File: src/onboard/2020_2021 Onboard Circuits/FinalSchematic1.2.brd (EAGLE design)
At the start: 135.6 x 80 mm, 99 parts, among them IC1 A5975D, IC2 A5975D, IC3 A5975D

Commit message: Removed 5V lines as one layer is a 5V pour so they were not needed because the components are through hole. Then updated photos of both boards
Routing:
- net 5V: track 329.9 -> 3.95 mm, vias 2 -> 0
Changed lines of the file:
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@@
 <vertex x="-35.56" y="78.105" curve="-90"/>
 </polygon>
-<via x="40.64" y="43.18" extent="1-16" drill="0.35"/>
 <contactref element="R52" pad="2"/>
 <contactref element="C12" pad="1"/>
 <contactref element="5V" pad="1"/>
 <contactref element="L2" pad="1"/>
-<wire x1="88.9" y1="73.66" x2="98.8824" y2="63.6776" width="0.2032" layer="1"/>
-<wire x1="98.8824" y1="36.6524" x2="97.79" y2="35.56" width="0.2032" layer="1"/>
-<wire x1="97.79" y1="35.56" x2="97.79" y2="34.29" width="0.2032" layer="1"/>
-<wire x1="98.8824" y1="63.6776" x2="98.8824" y2="36.6524" width="0.2032" layer="1"/>
-<wire x1="45.72" y1="55.63" x2="48.1076" y2="53.2424" width="0.2032" layer="16"/>
-<wire x1="48.1076" y1="53.2424" x2="48.1076" y2="48.4124" width="0.2032" layer="16"/>
-<wire x1="48.1076" y1="48.4124" x2="42.8752" y2="43.18" width="0.2032" layer="16"/>
-<wire x1="42.8752" y1="43.18" x2="40.64" y2="43.18" width="0.2032" layer="16"/>
 <contactref element="DIP_1_2" pad="3"/>
-<wire x1="34.827" y1="36.656" x2="34.827" y2="32.483" width="0.2032" layer="1"/>
-<wire x1="34.827" y1="36.656" x2="34.827" y2="36.83" width="0.2032" layer="1"/>
-<wire x1="34.827" y1="36.83" x2="34.827" y2="37.367" width="0.2032" layer="1"/>
-<wire x1="34.827" y1="37.367" x2="40.64" y2="43.18" width="0.2032" layer="1"/>
-<wire x1="88.9" y1="26.67" x2="88.9" y2="24.13" width="0.3048" layer="16"/>
-<wire x1="86.3882" y1="21.6182" x2="86.3882" y2="9.1158" width="0.3048" layer="16"/>
-<wire x1="90.17" y1="5.334" x2="86.3882" y2="9.1158" width="0.3048" layer="16"/>
-<wire x1="90.17" y1="5.334" x2="90.17" y2="3.81" width="0.3048" layer="16"/>
-<wire x1="88.9" y1="24.13" x2="86.3882" y2="21.6182" width="0.3048" layer="16"/>
-<wire x1="54.61" y1="19.05" x2="50.8" y2="22.86" width="0.3048" layer="1"/>
-<wire x1="50.8" y1="22.86" x2="50.8" y2="24.13" width="0.3048" layer="1"/>
-<wire x1="50.8" y1="24.13" x2="48.67829375" y2="24.13" width="0.3048" layer="1"/>
-<wire x1="48.67829375" y1="24.13" x2="47.48449375" y2="25.3238" width="0.3048" layer="1"/>
-<wire x1="47.48449375" y1="25.3238" x2="41.9862" y2="25.3238" width="0.3048" layer="1"/>
-<wire x1="41.9862" y1="25.3238" x2="34.827" y2="32.483" width="0.3048" layer="1"/>
-<wire x1="34.827" y1="32.483" x2="34.827" y2="36.83" width="0.3048" layer="1"/>
-<wire x1="26.6708" y1="28.6738" x2="34.827" y2="36.83" width="0.3048" layer="1"/>
-<wire x1="17.2438" y1="28.6738" x2="26.6708" y2="28.6738" width="0.3048" layer="1"/>
-<wire x1="10.16" y1="16.51" x2="10.16" y2="21.59" width="0.3048" layer="1"/>
-<wire x1="10.16" y1="21.59" x2="-6.35" y2="38.1" width="0.3048" layer="1"/>
-<wire x1="-6.35" y1="38.1" x2="-10.16" y2="38.1" width="0.3048" layer="1"/>
-<wire x1="-10.16" y1="38.1" x2="-12.7" y2="38.1" width="0.3048" layer="1"/>
-<wire x1="-16.01550625" y1="36.9062" x2="-17.00449375" y2="36.9062" width="0.3048" layer="1"/>
-<wire x1="-12.7" y1="38.1" x2="-14.82170625" y2="38.1" width="0.3048" layer="1"/>
-<wire x1="-18.19829375" y1="38.1" x2="-20.32" y2="38.1" width="0.3048" layer="1"/>
-<wire x1="-14.82170625" y1="38.1" x2="-16.01550625" y2="36.9062" width="0.3048" layer="1"/>
-<wire x1="-17.00449375" y1="36.9062" x2="-18.19829375" y2="38.1" width="0.3048" layer="1"/>
 <wire x1="-20.32" y1="38.1" x2="-22.843" y2="38.1" width="0.3048" layer="1"/>
 <wire x1="-22.843" y1="38.1" x2="-23.715" y2="38.972" width="0.3048" layer="1"/>
-<via x="20.32" y="15.24" extent="1-16" drill="0.35"/>
-<wire x1="20.32" y1="15.24" x2="20.4343" y2="15.3543" width="0.3048" layer="16"/>
-<wire x1="20.4343" y1="15.3543" x2="33.4987125" y2="15.3543" width="0.3048" layer="16"/>
-<wire x1="53.34" y1="17.78" x2="35.9244125" y2="17.78" width="0.3048" layer="16"/>
-<wire x1="33.4987125" y1="15.3543" x2="35.9244125" y2="17.78" width="0.3048" layer="16"/>
-<wire x1="54.61" y1="19.05" x2="53.34" y2="17.78" width="0.3048" layer="16"/>
-<wire x1="16.74225" y1="15.24" x2="8.89" y2="7.38775" width="0.3048" layer="1"/>
-<wire x1="8.89" y1="7.38775" x2="8.89" y2="3.556" width="0.3048" layer="1"/>
-<wire x1="16.74225" y1="15.24" x2="20.32" y2="15.24" width="0.3048" layer="1"/>
-<wire x1="97.79" y1="34.29" x2="92.0496" y2="28.5496" width="0.3048" layer="16"/>
-<wire x1="92.0496" y1="28.5496" x2="90.97706875" y2="28.5496" width="0.3048" layer="16"/>
 <wire x1="89.09746875" y1="26.67" x2="88.9" y2="26.67" width="0.3048" layer="16"/>
-<wire x1="90.97706875" y1="28.5496" x2="89.09746875" y2="26.67" width="0.3048" layer="16"/>
-<wire x1="88.9" y1="26.67" x2="83.2838" y2="21.0538" width="0.3048" layer="16"/>
-<wire x1="72.4888" y1="21.0538" x2="83.2838" y2="21.0538" width="0.3048" layer="16"/>
-<wire x1="68.58" y1="16.51" x2="68.58" y2="15.6044125" width="0.3048" layer="1"/>
-<wire x1="67.4243" y1="13.4493" x2="64.77" y2="10.795" width="0.3048" layer="1"/>
-<wire x1="68.58" y1="15.6044125" x2="67.4243" y2="14.4487125" width="0.3048" layer="1"/>
-<wire x1="67.4243" y1="14.4487125" x2="67.4243" y2="13.4493" width="0.3048" layer="1"/>
-<wire x1="64.77" y1="10.795" x2="66.04" y2="9.525" width="0.3048" layer="16"/>
-<wire x1="66.04" y1="9.525" x2="66.04" y2="2.54" width="0.3048" layer="16"/>
-<wire x1="64.77" y1="10.795" x2="62.865" y2="10.795" width="0.3048" layer="16"/>
-<wire x1="62.865" y1="10.795" x2="54.61" y2="19.05" width="0.3048" layer="16"/>
-<wire x1="10.16" y1="21.59" x2="17.2438" y2="28.6738" width="0.3048" layer="1"/>
-<wire x1="68.58" y1="16.51" x2="70.485" y2="18.415" width="0.3048" layer="16"/>
-<wire x1="70.485" y1="18.415" x2="70.485" y2="19.05" width="0.3048" layer="16"/>
-<wire x1="70.485" y1="19.05" x2="72.4888" y2="21.0538" width="0.3048" layer="16"/>
 </signal>
 <signal name="DIP1">
@@
 <wire x1="73.66" y1="16.51" x2="74.93" y2="15.24" width="0.1524" layer="16"/>
 <wire x1="74.93" y1="15.24" x2="74.93" y2="3.81" width="0.1524" layer="16"/>
-<wire x1="73.2286375" y1="16.7386" x2="70.2822375" y2="19.685" width="0.1524" layer="1"/>
-<wire x1="69.215" y1="19.685" x2="70.2822375" y2="19.685" width="0.1524" layer="1"/>
-<wire x1="73.2286375" y1="16.7386" x2="73.4314" y2="16.7386" width="0.1524" layer="1"/>
-<wire x1="73.4314" y1="16.7386" x2="73.66" y2="16.51" width="0.1524" layer="1"/>
+<wire x1="71.7046375" y1="17.7546" x2="69.7742375" y2="19.685" width="0.1524" layer="1"/>
+<wire x1="69.215" y1="19.685" x2="69.7742375" y2="19.685" width="0.1524" layer="1"/>
+<wire x1="71.7046375" y1="17.7546" x2="72.4154" y2="17.7546" width="0.1524" layer="1"/>
+<wire x1="72.4154" y1="17.7546" x2="73.66" y2="16.51" width="0.1524" layer="1"/>
 </signal>
 <signal name="BLUE">
@@
 <wire x1="74.295" y1="29.845" x2="69.85" y2="34.29" width="0.1524" layer="1"/>
 <via x="87.4381" y="18.161" extent="1-16" drill="0.35"/>
-<wire x1="93.98" y1="16.51" x2="92.7608" y2="17.7292" width="0.1524" layer="16"/>
-<wire x1="87.8699" y1="17.7292" x2="87.4381" y2="18.161" width="0.1524" layer="16"/>
-<wire x1="92.7608" y1="17.7292" x2="87.8699" y2="17.7292" width="0.1524" layer="16"/>
 <wire x1="87.4381" y1="18.161" x2="87.249" y2="18.161" width="0.1524" layer="1"/>
+<wire x1="87.4381" y1="18.161" x2="92.329" y2="18.161" width="0.1524" layer="16"/>
+<wire x1="92.329" y1="18.161" x2="93.98" y2="16.51" width="0.1524" layer="16"/>
 </signal>
 <signal name="O_LED">

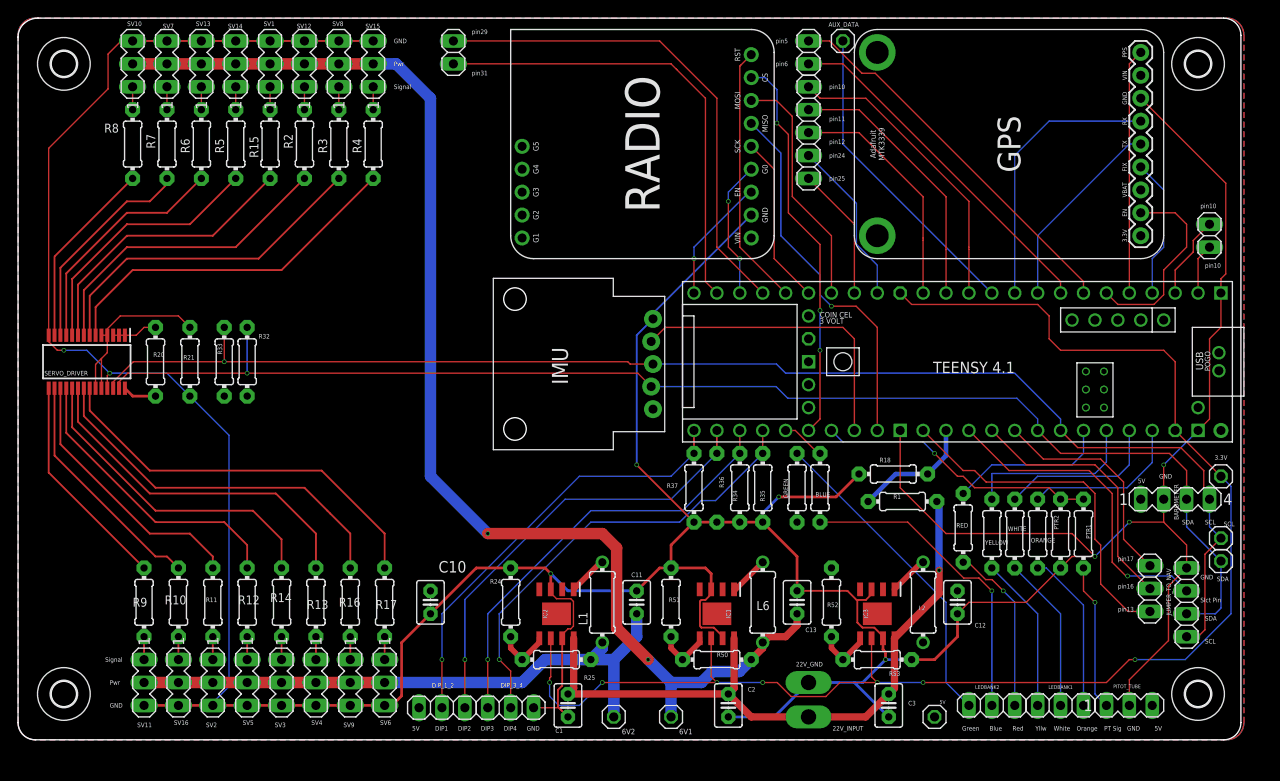
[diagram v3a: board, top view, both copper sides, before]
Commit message: Changed hole sizes for both board to 3mm for M3 screws and made boards slilghtly larger to have room around the holes without disrupting the wire traces. Updated photos of both boards.
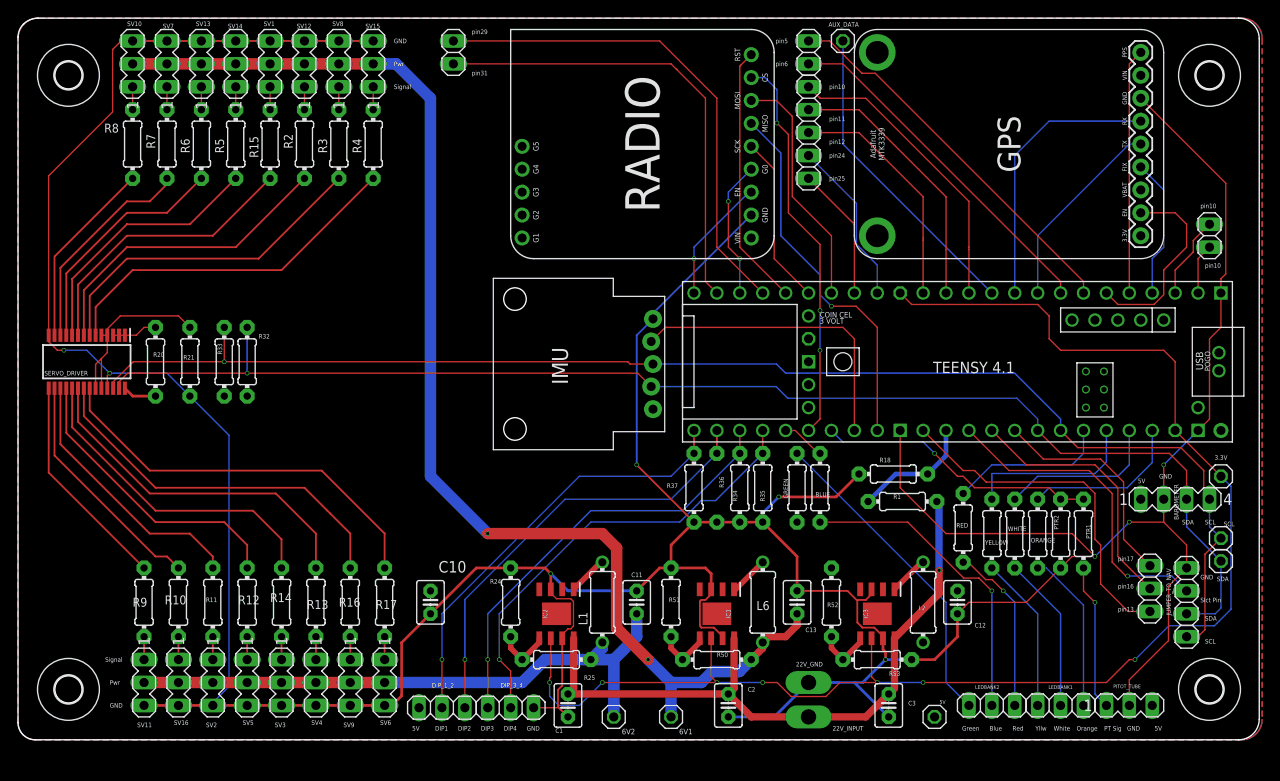
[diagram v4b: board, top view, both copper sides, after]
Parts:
- removed U$5: (no value), holes:2,8
- added U$2: (no value), holes:3,0
- U$1, U$3, U$4: device holes:2,8 -> holes:3,0
- moved U$1 144.7 mm to (96.5, 5.59)
- moved U$4 144.3 mm to (96.5, 73.7)
- moved U$3 125.2 mm to (-30.0, 73.7)
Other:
- board size 135.6 x 80 mm -> 137.6 x 80 mm
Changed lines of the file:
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@@
 <board>
 <plain>
-<wire x1="-33.655" y1="0" x2="98.095" y2="0" width="0" layer="20"/>
-<wire x1="98.095" y1="0" x2="100" y2="1.905" width="0" layer="20" curve="90"/>
-<wire x1="100" y1="1.905" x2="100" y2="78.095" width="0" layer="20"/>
-<wire x1="100" y1="78.095" x2="98.095" y2="80" width="0" layer="20" curve="90"/>
-<wire x1="98.095" y1="80" x2="-33.35310625" y2="80" width="0" layer="20"/>
+<wire x1="-33.655" y1="0" x2="99.746" y2="0" width="0" layer="20"/>
+<wire x1="99.746" y1="0" x2="102.032" y2="2.286" width="0" layer="20" curve="90"/>
+<wire x1="102.032" y1="2.286" x2="102.032" y2="77.714" width="0" layer="20"/>
+<wire x1="102.032" y1="77.714" x2="99.746" y2="80" width="0" layer="20" curve="90"/>
+<wire x1="99.746" y1="80" x2="-33.35310625" y2="80" width="0" layer="20"/>
 <wire x1="-33.35310625" y1="80" x2="-34.969553125" y2="79.330446875" width="0" layer="20" curve="45"/>
 <wire x1="-34.969553125" y1="79.330446875" x2="-35.56" y2="77.90498125" width="0" layer="20" curve="45"/>
@@
 <attribute name="VALUE" x="65.3596" y="13.4366" size="0.508" layer="27" ratio="10" rot="R180"/>
 </element>
-<element name="U$1" library="holes" library_urn="urn:adsk.eagle:library:237" package="2,8" package3d_urn="urn:adsk.eagle:package:14271/1" value="" x="-30.48" y="74.93" smashed="yes"/>
-<element name="U$3" library="holes" library_urn="urn:adsk.eagle:library:237" package="2,8" package3d_urn="urn:adsk.eagle:package:14271/1" value="" x="95.25" y="74.93" smashed="yes"/>
-<element name="U$4" library="holes" library_urn="urn:adsk.eagle:library:237" package="2,8" package3d_urn="urn:adsk.eagle:package:14271/1" value="" x="-30.48" y="5.08" smashed="yes"/>
-<element name="U$5" library="holes" library_urn="urn:adsk.eagle:library:237" package="2,8" package3d_urn="urn:adsk.eagle:package:14271/1" value="" x="95.25" y="5.08" smashed="yes"/>
 <element name="R24" library="adafruit" library_urn="urn:adsk.eagle:library:420" package="0204/7" package3d_urn="urn:adsk.eagle:package:6240596/1" value="1.5k" x="19.05" y="15.24" smashed="yes" rot="R270">
 <attribute name="NAME" x="16.764" y="17.2974" size="0.508" layer="25" ratio="12"/>
@@
 <attribute name="VALUE" x="86.741" y="20.574" size="1.27" layer="27" rot="R270"/>
 </element>
+<element name="U$1" library="holes" library_urn="urn:adsk.eagle:library:237" package="3,0" package3d_urn="urn:adsk.eagle:package:14277/1" value="" x="96.52" y="5.588" smashed="yes"/>
+<element name="U$2" library="holes" library_urn="urn:adsk.eagle:library:237" package="3,0" package3d_urn="urn:adsk.eagle:package:14277/1" value="" x="-29.972" y="5.588" smashed="yes"/>
+<element name="U$3" library="holes" library_urn="urn:adsk.eagle:library:237" package="3,0" package3d_urn="urn:adsk.eagle:package:14277/1" value="" x="-29.972" y="73.66" smashed="yes"/>
+<element name="U$4" library="holes" library_urn="urn:adsk.eagle:library:237" package="3,0" package3d_urn="urn:adsk.eagle:package:14277/1" value="" x="96.52" y="73.66" smashed="yes"/>
 </elements>
 <signals>
@@
 <contactref element="PITOT_TUBE" pad="3"/>
 <polygon width="0.3048" layer="16">
-<vertex x="-33.655" y="80.01"/>
-<vertex x="98.425" y="80.01" curve="-90"/>
-<vertex x="100.33" y="78.105"/>
-<vertex x="100.33" y="1.905" curve="-90"/>
-<vertex x="98.425" y="0"/>
+<vertex x="-35.56" y="1.905"/>
+<vertex x="-35.56" y="77.724" curve="-90"/>
+<vertex x="-33.274" y="80.01"/>
+<vertex x="100.076" y="80.01" curve="-90"/>
+<vertex x="102.362" y="77.724"/>
+<vertex x="102.362" y="2.286" curve="-90"/>
+<vertex x="100.076" y="0"/>
 <vertex x="-33.655" y="0" curve="-90"/>
-<vertex x="-35.56" y="1.905"/>
-<vertex x="-35.56" y="78.105" curve="-90"/>
 </polygon>
 <contactref element="R52" pad="2"/>
@@
 <wire x1="92.71" y1="41.91" x2="92.71" y2="34.29" width="0.1524" layer="1"/>
 <wire x1="97.79" y1="29.21" x2="98.9078" y2="28.0922" width="0.1524" layer="16"/>
-<wire x1="98.9078" y1="28.0922" x2="98.9078" y2="13.97" width="0.1524" layer="16"/>
+<wire x1="98.9078" y1="28.0922" x2="98.9078" y2="14.478" width="0.1524" layer="16"/>
 <contactref element="IC1" pad="6"/>
 <contactref element="IC3" pad="6"/>
-<wire x1="98.9078" y1="13.97" x2="93.8278" y2="8.89" width="0.1524" layer="16"/>
-<wire x1="93.8278" y1="8.89" x2="88.265" y2="8.89" width="0.1524" layer="16"/>
+<wire x1="98.9078" y1="14.478" x2="97.5869" y2="13.1571" width="0.1524" layer="16"/>
+<wire x1="97.5869" y1="13.1571" x2="97.3838" y2="12.954" width="0.1524" layer="16"/>
 <via x="88.265" y="8.89" extent="1-16" drill="0.35"/>
 <via x="64.77" y="6.35" extent="1-16" drill="0.35"/>
+<wire x1="92.0115" y1="12.6365" x2="88.265" y2="8.89" width="0.1524" layer="16"/>
 <wire x1="85.09" y1="6.35" x2="64.77" y2="6.35" width="0.1524" layer="1"/>
 <wire x1="88.265" y1="8.89" x2="87.63" y2="8.89" width="0.1524" layer="1"/>
@@
 <wire x1="23.368" y1="6.858" x2="23.368" y2="6.35" width="0.1524" layer="1"/>
 <wire x1="29.21" y1="6.35" x2="41.91" y2="6.35" width="0.1524" layer="1"/>
+<wire x1="97.3838" y1="12.954" x2="97.0663" y2="12.6365" width="0.1524" layer="16"/>
+<wire x1="97.0663" y1="12.6365" x2="92.0115" y2="12.6365" width="0.1524" layer="16"/>
 </signal>
 <signal name="PWM0">
@@
 <wire x1="95.25" y1="34.29" x2="91.44" y2="30.48" width="0.1524" layer="16"/>
 <polygon width="0.3048" layer="1">
-<vertex x="-33.655" y="80.01"/>
-<vertex x="98.425" y="80.01" curve="-90"/>
-<vertex x="100.33" y="78.105"/>
-<vertex x="100.33" y="1.905" curve="-90"/>
-<vertex x="98.425" y="0"/>
+<vertex x="-35.56" y="1.905"/>
+<vertex x="-35.56" y="77.724" curve="-90"/>
+<vertex x="-33.274" y="80.01"/>
+<vertex x="100.076" y="80.01" curve="-90"/>
+<vertex x="102.362" y="77.724"/>
+<vertex x="102.362" y="2.286" curve="-90"/>
+<vertex x="100.076" y="0"/>
 <vertex x="-33.655" y="0" curve="-90"/>
-<vertex x="-35.56" y="1.905"/>
-<vertex x="-35.56" y="78.105" curve="-90"/>
 </polygon>
 <wire x1="97.79" y1="49.53" x2="97.79" y2="45.72" width="0.1524" layer="1"/>
@@
 <wire x1="83.82" y1="20.32" x2="81.28" y2="22.86" width="0.1524" layer="1"/>
 <wire x1="81.28" y1="22.86" x2="67.31" y2="22.86" width="0.1524" layer="1"/>
-<wire x1="-25.5778" y1="72.1554875" x2="-25.5778" y2="76.0222" width="0.1524" layer="1"/>
-<wire x1="-32.165" y1="44.848" x2="-32.165" y2="65.5682875" width="0.1524" layer="1"/>
-<wire x1="-32.165" y1="65.5682875" x2="-25.5778" y2="72.1554875" width="0.1524" layer="1"/>
-<wire x1="-25.5778" y1="76.0222" x2="-24.13" y2="77.47" width="0.1524" layer="1"/>
+<wire x1="-25.0698" y1="69.6154875" x2="-25.0698" y2="76.5302" width="0.1524" layer="1"/>
+<wire x1="-32.165" y1="44.848" x2="-32.165" y2="62.5202875" width="0.1524" layer="1"/>
+<wire x1="-32.165" y1="62.5202875" x2="-25.0698" y2="69.6154875" width="0.1524" layer="1"/>
+<wire x1="-25.0698" y1="76.5302" x2="-24.13" y2="77.47" width="0.1524" layer="1"/>
 <wire x1="81.28" y1="20.32" x2="83.82" y2="20.32" width="0.1524" layer="1"/>
 <wire x1="81.28" y1="20.32" x2="80.01" y2="19.05" width="0.1524" layer="1"/>
